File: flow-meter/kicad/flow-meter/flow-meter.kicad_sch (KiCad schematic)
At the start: 19 parts, among them J1 Screw_Terminal_01x03, Q1 2N7000, U1 DS18B20, U3 NodeMCU1.0(ESP-12E)

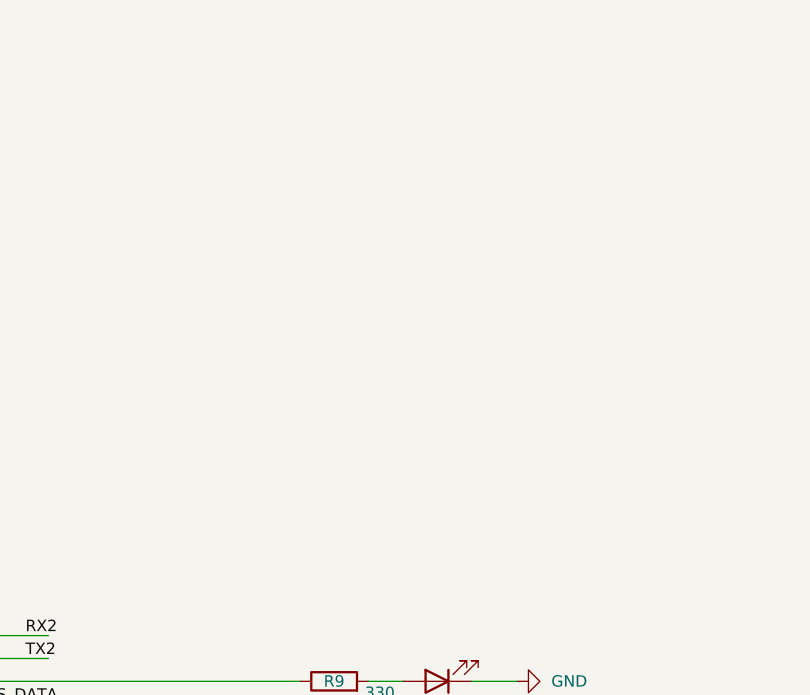
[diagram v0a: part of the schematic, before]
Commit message: flow-meter: update schematics
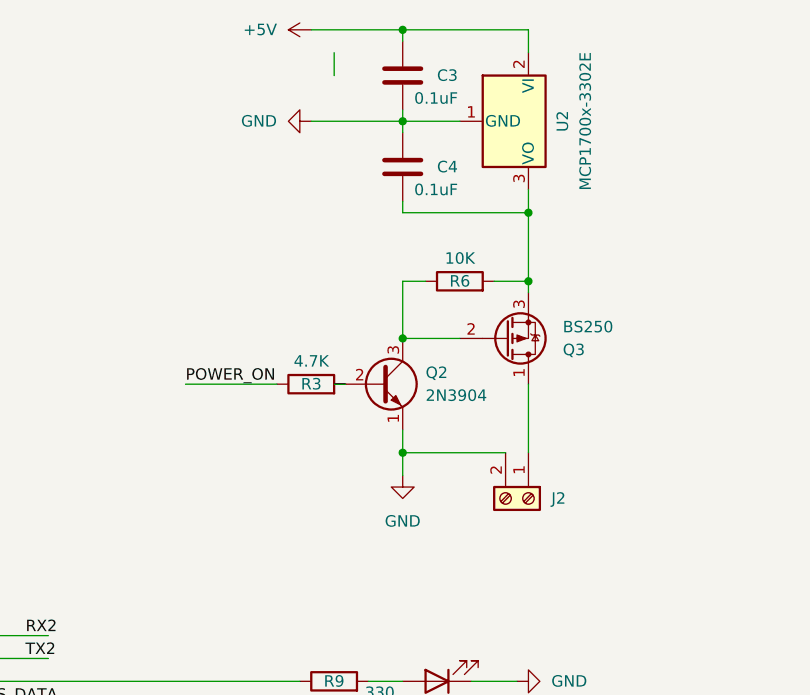
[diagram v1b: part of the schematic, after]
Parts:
- added C3, C4: 0.1uF, symbol Device:C
- added J2: Screw_Terminal_01x02, symbol Connector:Screw_Terminal_01x02
- added Q2: 2N3904, Package_TO_SOT_THT:TO-92_Inline, symbol Transistor_BJT:2N3904
- added Q3: BS250, Package_TO_SOT_THT:TO-92_Inline, symbol Transistor_FET:BS250
- added R3: 4.7K, symbol Device:R
- added R6: 10K, symbol Device:R
- added U2: MCP1700x-3302E, Package_TO_SOT_THT:TO-92_Inline, symbol Regulator_Linear:MCP1700x-330xxTO
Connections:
- net +5V: now also C3.1, U2.2 (VI)
- net GND: now also C3.2, C4.1, J2.2 (Pin_2), Q2.1 (E), U2.1 (GND)
- new net: Q2.2 (B), R3.2
- new net: Q2.3 (C), Q3.2 (G), R6.1
- new net: C4.2, Q3.3 (S), R6.2, U2.3 (VO)
- new net: J2.1 (Pin_1), Q3.1 (D)
- new net POWER_ON: R3.1
